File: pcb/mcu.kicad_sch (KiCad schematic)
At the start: 0 parts

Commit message: Added ESP32S3 Mini Signed-off-by: Damir Gazizullin <dgazizul@uwaterloo.ca>
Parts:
- added U1: ESP32-S3-MINI-1, RF_Module:ESP32-S2-MINI-1, symbol RF_Module:ESP32-S3-MINI-1
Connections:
- new net: U1.1 (GND), U1.2 (GND), U1.42 (GND), U1.43 (GND), U1.46 (GND), U1.47 (GND), U1.48 (GND), U1.49 (GND), U1.50 (GND), U1.51 (GND), U1.52 (GND), U1.53 (GND), U1.54 (GND), U1.55 (GND), U1.56 (GND), U1.57 (GND), U1.58 (GND), U1.59 (GND), U1.60 (GND), U1.61 (GND), U1.62 (GND), U1.63 (GND), U1.64 (GND), U1.65 (GND)
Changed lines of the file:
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@@
 	(generator_version "9.0")
 	(paper "A4")
+	(symbol
+		(lib_id "RF_Module:ESP32-S3-MINI-1")
+		(at 72.39 76.2 0)
+		(unit 1)
+		(exclude_from_sim no)
+		(in_bom yes)
+		(on_board yes)
+		(dnp no)
+		(fields_autoplaced yes)
+		(property "Reference" "U1"
+			(at 74.5333 43.18 0)
+			(effects
+				(font
+					(size 1.27 1.27)
+				)
+				(justify left)
+			)
+		)
+		(property "Value" "ESP32-S3-MINI-1"
+			(at 74.5333 45.72 0)
+			(effects
+				(font
+					(size 1.27 1.27)
+				)
+				(justify left)
+			)
+		)
+		(property "Footprint" "RF_Module:ESP32-S2-MINI-1"
+			(at 87.63 105.41 0)
+			(effects
+				(font
+					(size 1.27 1.27)
+				)
+				(hide yes)
+			)
+		)
+		(property "Datasheet" "https://www.espressif.com/sites/default/files/documentation/esp32-s3-mini-1_mini-1u_datasheet_en.pdf"
+			(at 72.39 35.56 0)
+			(effects
+				(font
+					(size 1.27 1.27)
+				)
+				(hide yes)
+			)
+		)
+		(property "Description" "RF Module, ESP32-S3 SoC, Wi-Fi 802.11b/g/n, Bluetooth, BLE, 32-bit, 3.3V, SMD, onboard antenna"
+			(at 72.39 33.02 0)
+			(effects
+				(font
+					(size 1.27 1.27)
+				)
+				(hide yes)
+			)
+		)
+		(pin "11"
+		)
+		(pin "8"
+		)
+		(pin "20"
+		)
+		(pin "3"
+		)
+		(pin "43"
+		)
+		(pin "6"
+		)
+		(pin "47"
+		)
+		(pin "45"
+		)
+		(pin "9"
+		)
+		(pin "4"
+		)
+		(pin "10"
+		)
+		(pin "12"
+		)
+		(pin "14"
+		)
+		(pin "13"
+		)
+		(pin "18"
+		)
+		(pin "19"
+		)
+		(pin "21"
+		)
+		(pin "7"
+		)
+		(pin "17"
+		)
+		(pin "15"
+		)
+		(pin "42"
+		)
+		(pin "5"
+		)
+		(pin "2"
+		)
+		(pin "16"
+		)
+		(pin "22"
+		)
+		(pin "1"
+		)
+		(pin "46"
+		)
+		(pin "48"
+		)
+		(pin "49"
+		)
+		(pin "39"
+		)
+		(pin "57"
+		)
+		(pin "31"
+		)
+		(pin "56"
+		)
+		(pin "35"
+		)
+		(pin "51"
+		)
+		(pin "58"
+		)
+		(pin "50"
+		)
+		(pin "52"
+		)
+		(pin "60"
+		)
+		(pin "62"
+		)
+		(pin "65"
+		)
+		(pin "40"
+		)
+		(pin "55"
+		)
+		(pin "23"
+		)
+		(pin "24"
+		)
+		(pin "54"
+		)
+		(pin "64"
+		)
+		(pin "28"
+		)
+		(pin "29"
+		)
+		(pin "59"
+		)
+		(pin "61"
+		)
+		(pin "63"
+		)
+		(pin "53"
+		)
+		(pin "25"
+		)
+		(pin "26"
+		)
+		(pin "32"
+		)
+		(pin "33"
+		)
+		(pin "34"
+		)
+		(pin "44"
+		)
+		(pin "27"
+		)
+		(pin "30"
+		)
+		(pin "37"
+		)
+		(pin "36"
+		)
+		(pin "38"
+		)
+		(pin "41"
+		)
+		(instances
+			(project ""
+				(path "/5072676b-6ffc-4812-9165-a6d5aae17d98/1c391981-fffe-4c54-847d-b61b4420497c"
+					(reference "U1")
+					(unit 1)
+				)
+			)
+		)
+	)
 )

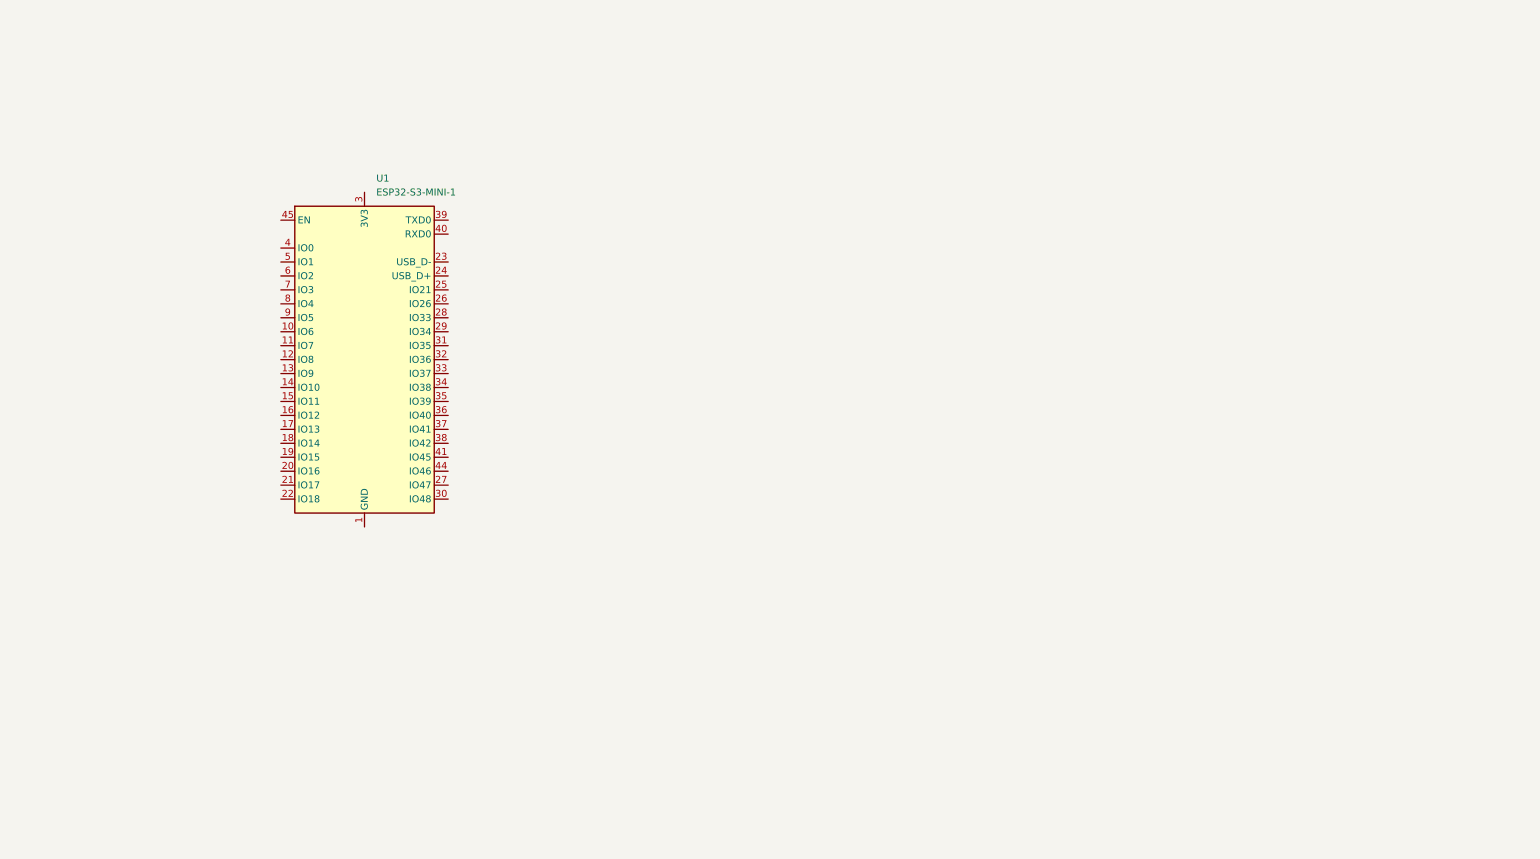
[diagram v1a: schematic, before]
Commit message: Refactored Pins for MCU, added button component footprint Signed-off-by: Damir Gazizullin <dgazizul@uwaterloo.ca>
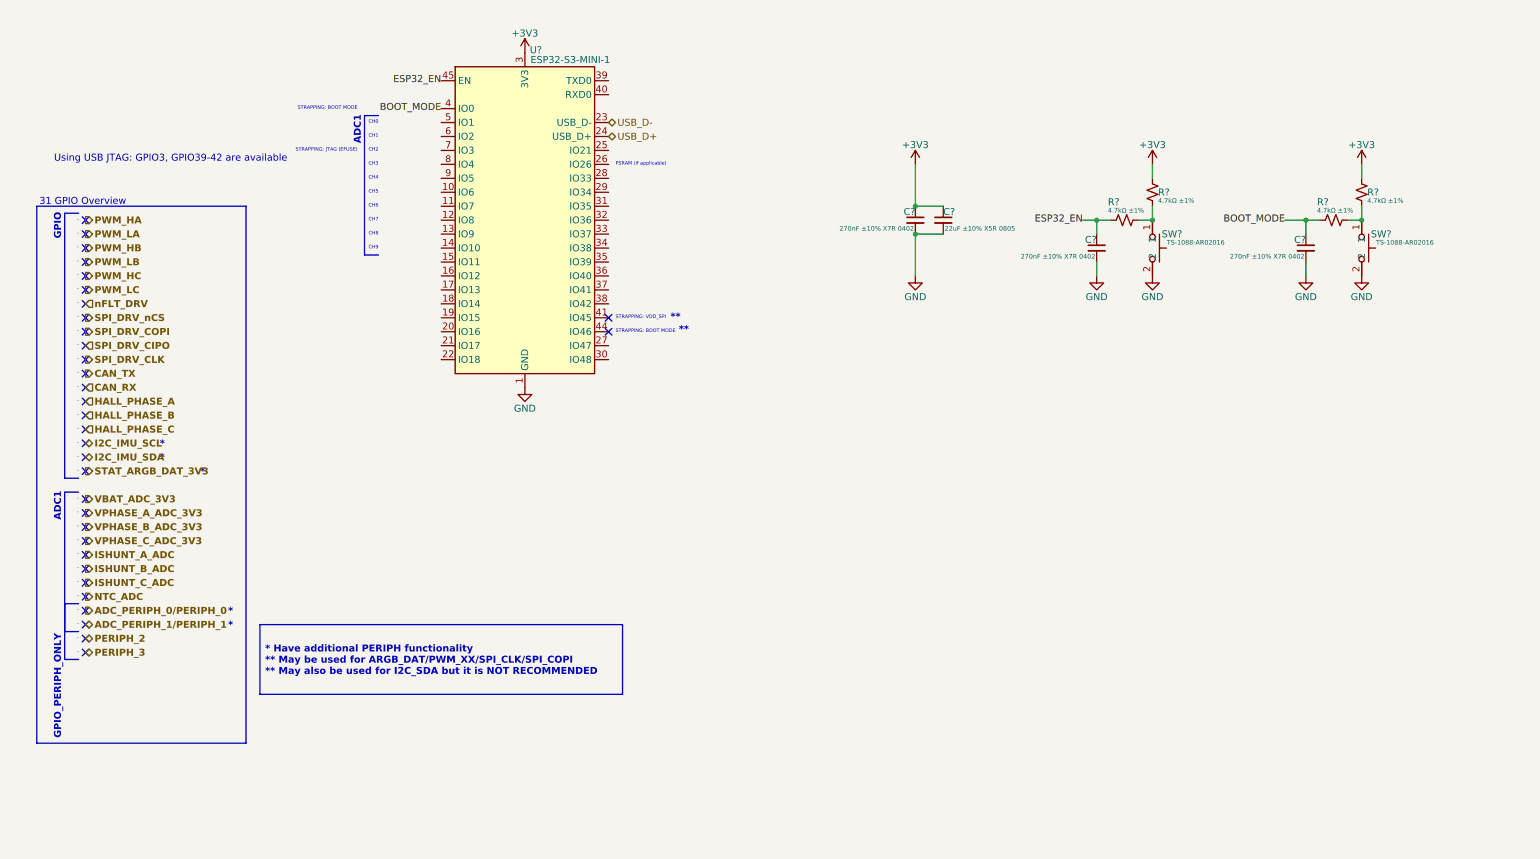
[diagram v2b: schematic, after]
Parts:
- added C?: 22uF ±10% X5R 0805, Capacitor_SMD:C_0805_2012Metric, symbol Device:C_Small
- added C? (x3): 270nF ±10% X7R 0402, Capacitor_SMD:C_0402_1005Metric, symbol Device:C_Small
- added R? (x4): 4.7kΩ ±1%, Resistor_SMD:R_0402_1005Metric, symbol Device:R_Small_US
- added SW? (x2): TS-1088-AR02016, TS-1088-AR02016:SW-SMD_L3.9-W3.0-P4.45, symbol TS-1088-AR02016:TS-1088-AR02016
- renumbered U1 to U?
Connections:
- net GND: now reaches U?.1 (GND), U?.2 (GND), U?.42 (GND), U?.43 (GND), U?.46 (GND), U?.47 (GND), U?.48 (GND), U?.49 (GND), U?.50 (GND), U?.51 (GND), U?.52 (GND), U?.53 (GND), U?.54 (GND), U?.55 (GND), U?.56 (GND), U?.57 (GND), U?.58 (GND), U?.59 (GND), U?.60 (GND), U?.61 (GND), U?.62 (GND), U?.63 (GND), U?.64 (GND), U?.65 (GND)
- net GND: now also C?.2, C?.2, C?.2, C?.2, SW?.2, SW?.2
- net USB_D-: now reaches U?.23 (USB_D-)
- net USB_D+: now reaches U?.24 (USB_D+)
- net +3V3: now reaches U?.3 (3V3)
- net +3V3: now also C?.1, C?.1, R?.1, R?.1
- net BOOT_MODE: now reaches U?.4 (IO0)
- net BOOT_MODE: now also C?.1, R?.1
- net ESP32_EN: now reaches U?.45 (EN)
- net ESP32_EN: now also C?.1, R?.1
- new net: R?.2, R?.2, SW?.1 (x2)
- no-connect marks 0 -> 33
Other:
- note added: "*"
- note added: "**"
- note added: "-"
- note added: "31 GPIO Overview"
- note added: "ADC1"
- note added: "CH0"
- note added: "CH1"
- note added: "CH2"
- note added: "CH3"
- note added: "CH4"
- note added: "CH5"
- note added: "CH6"
- note added: "CH7"
- note added: "CH8"
- note added: "CH9"
- note added: "GPIO"
- note added: "GPIO_PERIPH_ONLY"
- note added: "PSRAM (if applicable)"
- note added: "STRAPPING: BOOT MODE"
- note added: "STRAPPING: JTAG (EFUSE)"
- note added: "STRAPPING: VDD_SPI"
- note added: "Using USB JTAG: GPIO3, GPIO39-42 are available"
- moved on the sheet: U?

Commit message: Cleaned up Driver and added decaps
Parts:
- gave numbers to parts that had none: 11
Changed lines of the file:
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@@
 		(on_board yes)
 		(dnp no)
-		(property "Reference" "#PWR?"
+		(property "Reference" "#PWR08"
 			(at 243.84 67.31 0)
 			(effects
@@
 			(project "sresc"
 				(path "/5072676b-6ffc-4812-9165-a6d5aae17d98/1c391981-fffe-4c54-847d-b61b4420497c"
-					(reference "#PWR?")
+					(reference "#PWR08")
 					(unit 1)
 				)
@@
 		(on_board yes)
 		(dnp no)
-		(property "Reference" "#PWR03"
+		(property "Reference" "#PWR06"
 			(at 215.9 44.45 0)
 			(effects
@@
 			(project "sresc"
 				(path "/5072676b-6ffc-4812-9165-a6d5aae17d98/1c391981-fffe-4c54-847d-b61b4420497c"
-					(reference "#PWR03")
+					(reference "#PWR06")
 					(unit 1)
 				)
@@
 		(on_board yes)
 		(dnp no)
-		(property "Reference" "SW?"
+		(property "Reference" "SW2"
 			(at 257.556 53.34 90)
 			(effects
@@
 			(project "sresc"
 				(path "/5072676b-6ffc-4812-9165-a6d5aae17d98/1c391981-fffe-4c54-847d-b61b4420497c"
-					(reference "SW?")
+					(reference "SW2")
 					(unit 1)
 				)
@@
 		(on_board yes)
 		(dnp no)
-		(property "Reference" "#PWR04"
+		(property "Reference" "#PWR09"
 			(at 254 44.45 0)
 			(effects
@@
 			(project "sresc"
 				(path "/5072676b-6ffc-4812-9165-a6d5aae17d98/1c391981-fffe-4c54-847d-b61b4420497c"
-					(reference "#PWR04")
+					(reference "#PWR09")
 					(unit 1)
 				)
@@
 		(on_board yes)
 		(dnp no)
-		(property "Reference" "C?"
+		(property "Reference" "C2"
 			(at 177.8 49.276 0)
 			(effects
@@
 			(project "sresc"
 				(path "/5072676b-6ffc-4812-9165-a6d5aae17d98/1c391981-fffe-4c54-847d-b61b4420497c"
-					(reference "C?")
+					(reference "C2")
 					(unit 1)
 				)
@@
 		(on_board yes)
 		(dnp no)
-		(property "Reference" "SW?"
+		(property "Reference" "SW1"
 			(at 219.456 53.34 90)
 			(effects
@@
 			(project "sresc"
 				(path "/5072676b-6ffc-4812-9165-a6d5aae17d98/1c391981-fffe-4c54-847d-b61b4420497c"
-					(reference "SW?")
+					(reference "SW1")
 					(unit 1)
 				)
@@
 		(on_board yes)
 		(dnp no)
-		(property "Reference" "#PWR?"
+		(property "Reference" "#PWR04"
 			(at 172.72 67.31 0)
 			(effects
@@
 			(project "sresc"
 				(path "/5072676b-6ffc-4812-9165-a6d5aae17d98/1c391981-fffe-4c54-847d-b61b4420497c"
-					(reference "#PWR?")
+					(reference "#PWR04")
 					(unit 1)
 				)
@@
 		(on_board yes)
 		(dnp no)
-		(property "Reference" "#PWR02"
+		(property "Reference" "#PWR03"
 			(at 172.72 44.45 0)
 			(effects
@@
 			(project "sresc"
 				(path "/5072676b-6ffc-4812-9165-a6d5aae17d98/1c391981-fffe-4c54-847d-b61b4420497c"
-					(reference "#PWR02")
+					(reference "#PWR03")
 					(unit 1)
 				)
@@
 		(on_board yes)
 		(dnp no)
-		(property "Reference" "#PWR?"
+		(property "Reference" "#PWR07"
 			(at 215.9 67.31 0)
 			(effects
@@
 			(project "sresc"
 				(path "/5072676b-6ffc-4812-9165-a6d5aae17d98/1c391981-fffe-4c54-847d-b61b4420497c"
-					(reference "#PWR?")
+					(reference "#PWR07")
 					(unit 1)
 				)
@@
 		(on_board yes)
 		(dnp no)
-		(property "Reference" "R?"
+		(property "Reference" "R1"
 			(at 207.772 47.498 90)
 			(effects
@@
 			(project "sresc"
 				(path "/5072676b-6ffc-4812-9165-a6d5aae17d98/1c391981-fffe-4c54-847d-b61b4420497c"
-					(reference "R?")
+					(reference "R1")
 					(unit 1)
 				)
@@
 		(on_board yes)
 		(dnp no)
-		(property "Reference" "C?"
+		(property "Reference" "C4"
 			(at 243.84 54.356 0)
 			(effects
@@
 			(project "sresc"
 				(path "/5072676b-6ffc-4812-9165-a6d5aae17d98/1c391981-fffe-4c54-847d-b61b4420497c"
-					(reference "C?")
+					(reference "C4")
 					(unit 1)
 				)
@@
 		(on_board yes)
 		(dnp no)
-		(property "Reference" "U?"
+		(property "Reference" "U1"
 			(at 102.5047 19.812 0)
 			(effects
@@
 			(project ""
 				(path "/5072676b-6ffc-4812-9165-a6d5aae17d98/1c391981-fffe-4c54-847d-b61b4420497c"
-					(reference "U?")
+					(reference "U1")
 					(unit 1)
 				)
@@
 		(on_board yes)
 		(dnp no)
-		(property "Reference" "R?"
+		(property "Reference" "R2"
 			(at 216.916 45.72 0)
 			(effects
@@
 			(project "sresc"
 				(path "/5072676b-6ffc-4812-9165-a6d5aae17d98/1c391981-fffe-4c54-847d-b61b4420497c"
-					(reference "R?")
+					(reference "R2")
 					(unit 1)
 				)
@@
 		(on_board yes)
 		(dnp no)
-		(property "Reference" "#PWR?"
+		(property "Reference" "#PWR010"
 			(at 254 67.31 0)
 			(effects
@@
 			(project "sresc"
 				(path "/5072676b-6ffc-4812-9165-a6d5aae17d98/1c391981-fffe-4c54-847d-b61b4420497c"
-					(reference "#PWR?")
+					(reference "#PWR010")
 					(unit 1)
 				)
@@
 		(on_board yes)
 		(dnp no)
-		(property "Reference" "#PWR?"
+		(property "Reference" "#PWR05"
 			(at 205.74 67.31 0)
 			(effects
@@
 			(project "sresc"
 				(path "/5072676b-6ffc-4812-9165-a6d5aae17d98/1c391981-fffe-4c54-847d-b61b4420497c"
-					(reference "#PWR?")
+					(reference "#PWR05")
 					(unit 1)
 				)
@@
 		(on_board yes)
 		(dnp no)
-		(property "Reference" "R?"
+		(property "Reference" "R3"
 			(at 245.872 47.498 90)
 			(effects
@@
 			(project "sresc"
 				(path "/5072676b-6ffc-4812-9165-a6d5aae17d98/1c391981-fffe-4c54-847d-b61b4420497c"
-					(reference "R?")
+					(reference "R3")
 					(unit 1)
 				)
@@
 		(on_board yes)
 		(dnp no)
-		(property "Reference" "C?"
+		(property "Reference" "C1"
 			(at 172.72 49.276 0)
 			(effects
@@
 			(project "sresc"
 				(path "/5072676b-6ffc-4812-9165-a6d5aae17d98/1c391981-fffe-4c54-847d-b61b4420497c"
-					(reference "C?")
+					(reference "C1")
 					(unit 1)
 				)
@@
 		(on_board yes)
 		(dnp no)
-		(property "Reference" "#PWR?"
+		(property "Reference" "#PWR02"
 			(at 101.6 87.63 0)
 			(effects
@@
 			(project "sresc"
 				(path "/5072676b-6ffc-4812-9165-a6d5aae17d98/1c391981-fffe-4c54-847d-b61b4420497c"
-					(reference "#PWR?")
+					(reference "#PWR02")
 					(unit 1)
 				)
@@
 		(on_board yes)
 		(dnp no)
-		(property "Reference" "R?"
+		(property "Reference" "R4"
 			(at 255.016 45.72 0)
 			(effects
@@
 			(project "sresc"
 				(path "/5072676b-6ffc-4812-9165-a6d5aae17d98/1c391981-fffe-4c54-847d-b61b4420497c"
-					(reference "R?")
+					(reference "R4")
 					(unit 1)
 				)
@@
 		(on_board yes)
 		(dnp no)
-		(property "Reference" "C?"
+		(property "Reference" "C3"
 			(at 205.74 54.356 0)
 			(effects
@@
 			(project "sresc"
 				(path "/5072676b-6ffc-4812-9165-a6d5aae17d98/1c391981-fffe-4c54-847d-b61b4420497c"
-					(reference "C?")
-					(unit 1)
-				)
+					(reference "C3")
+					(unit 1)
+				)

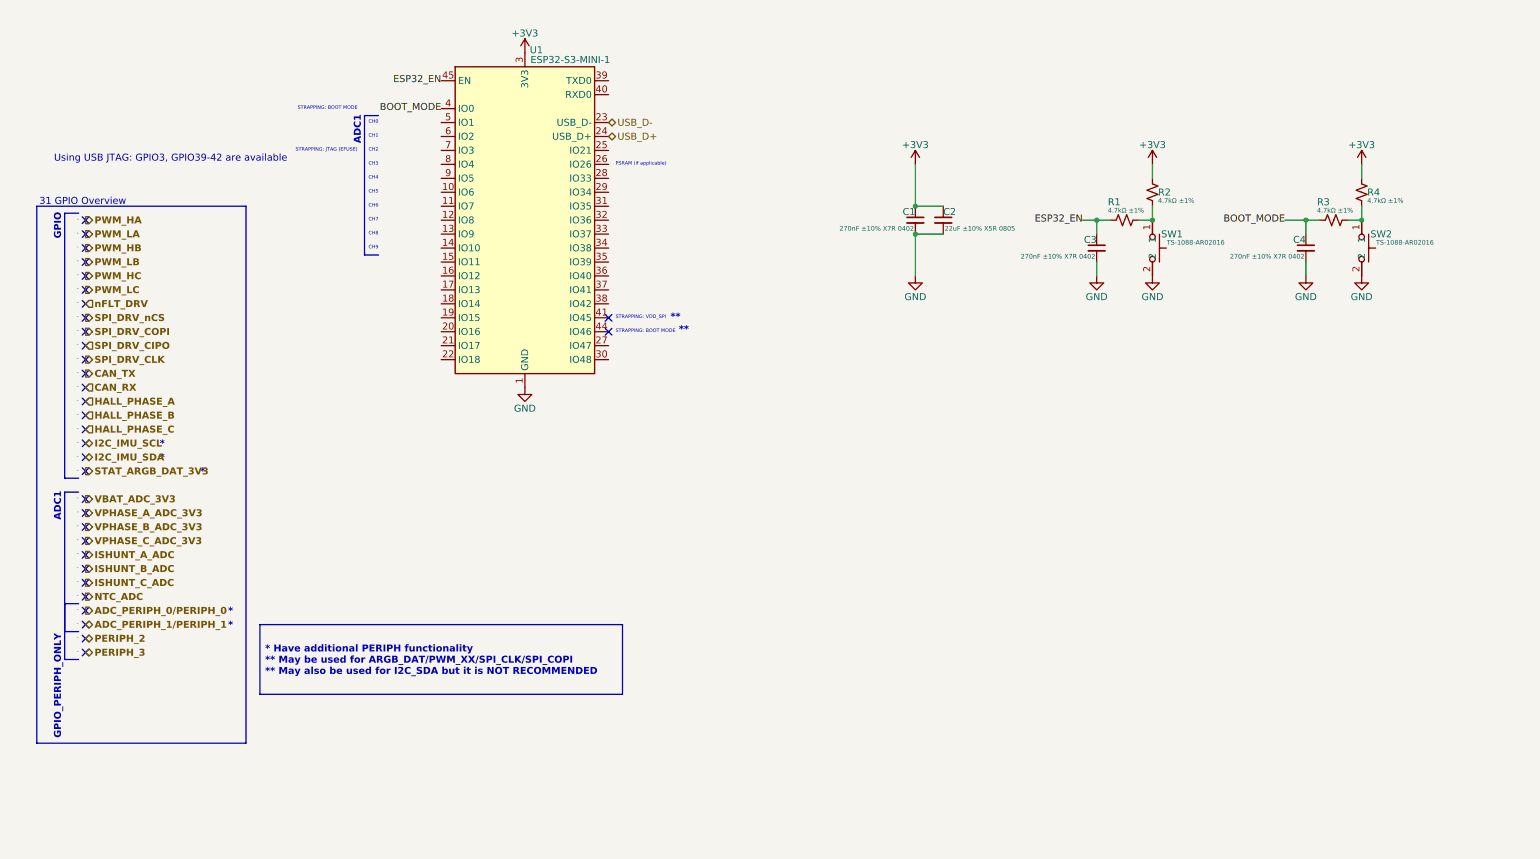
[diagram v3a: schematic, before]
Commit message: Add symbol/footprint libraries and update peripherals.kicad_sch
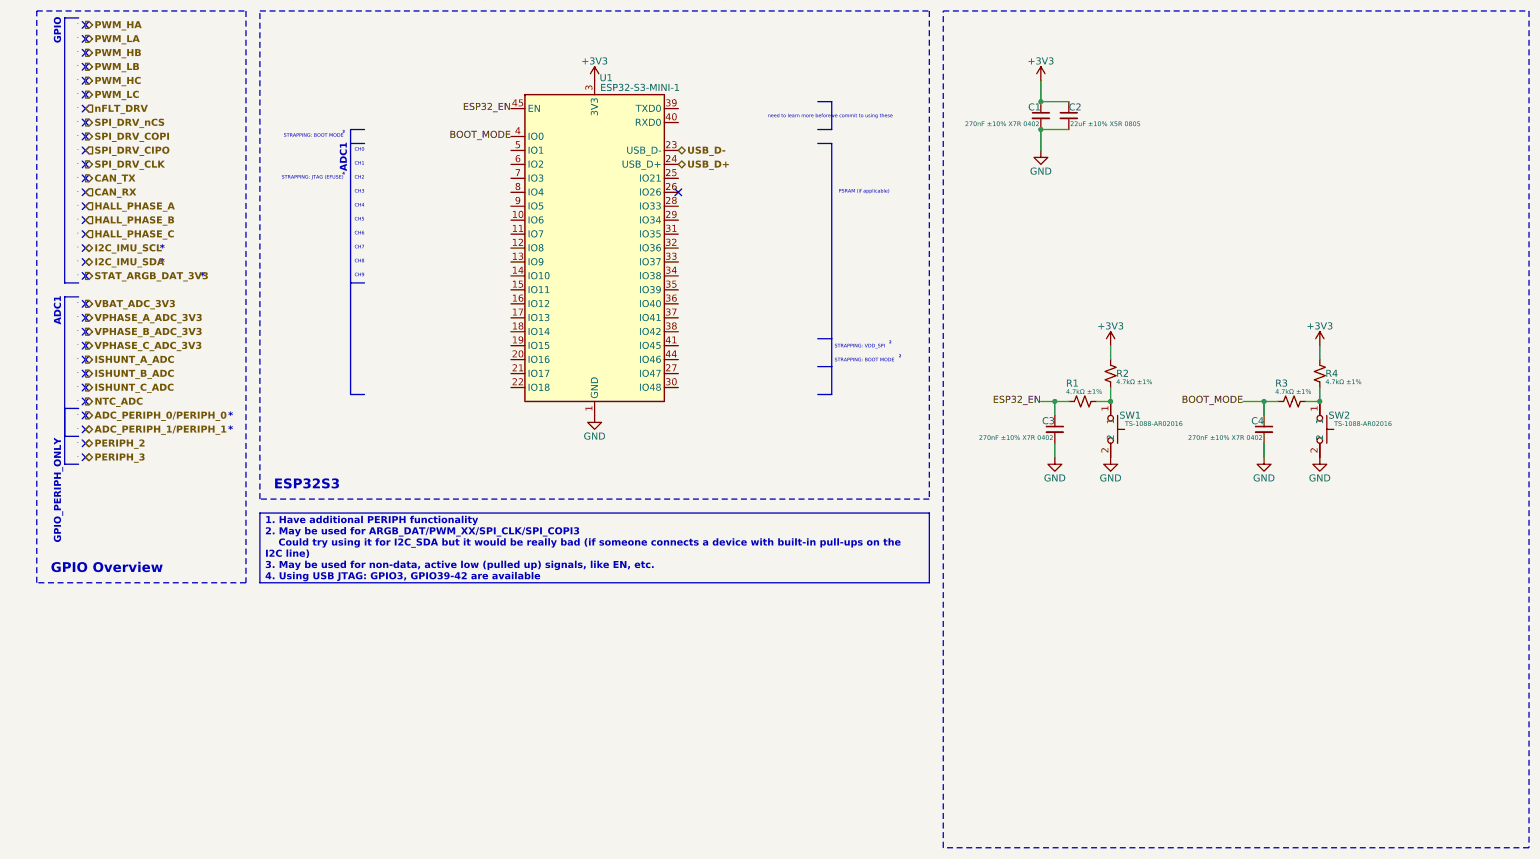
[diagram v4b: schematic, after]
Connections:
- no-connect marks 33 -> 32
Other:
- note added: "ESP32S3"
- note added: "GPIO Overview"
- note added: "^{2}"
- note added: "^{3}"
- note added: "^{4}"
- note added: "need to learn more beforewe commit to using these"
- note removed: "**"
- note removed: "31 GPIO Overview"
- note removed: "Using USB JTAG: GPIO3, GPIO39-42 are available"
- moved on the sheet: C1, C2, C3, C4, R1, R2, R3, R4, SW1, SW2, U1
